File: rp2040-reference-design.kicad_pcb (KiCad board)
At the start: 4 copper layers, 29.5 x 27 mm, 36 parts, among them J2 Conn_01x10_Pin, J3 Conn_01x10_Pin, U1 RP2040, U2 W25Q128JVS, Y1 12mhz ABM8-272-T

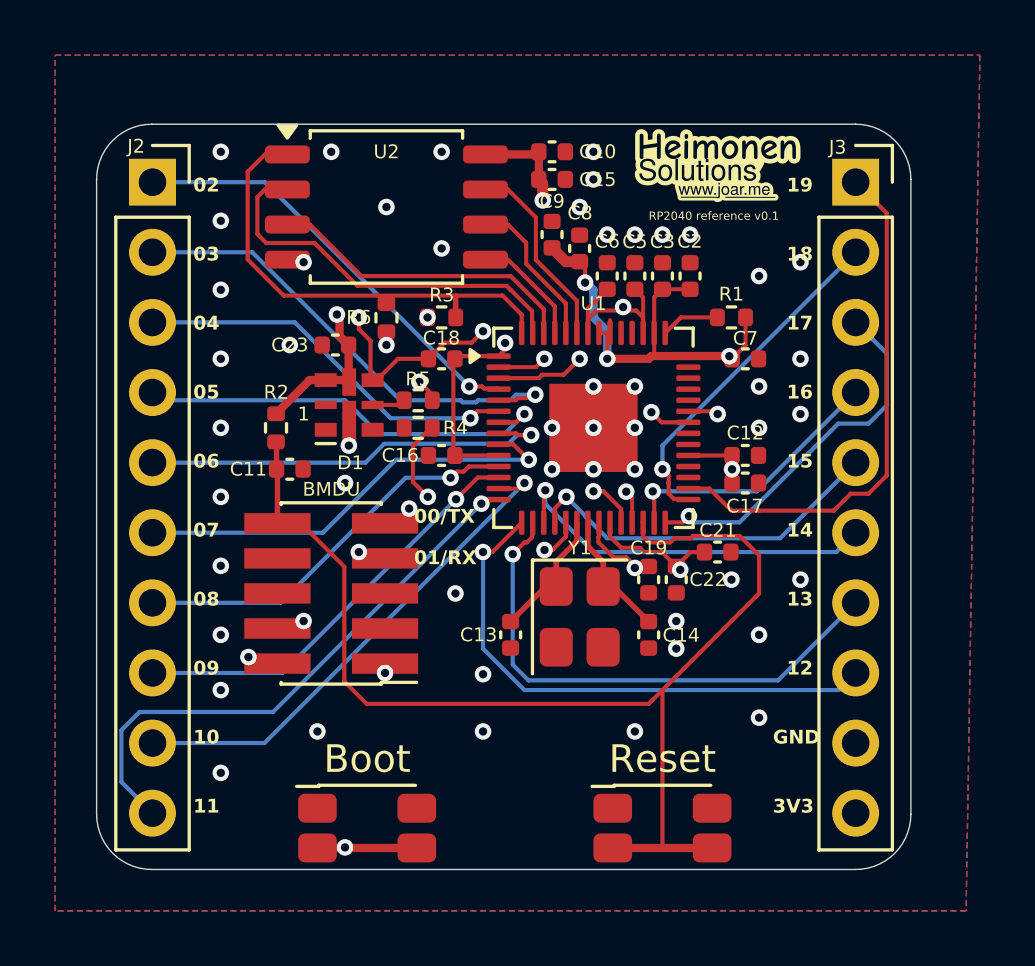
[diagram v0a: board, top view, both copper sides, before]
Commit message: fix: grounded cap
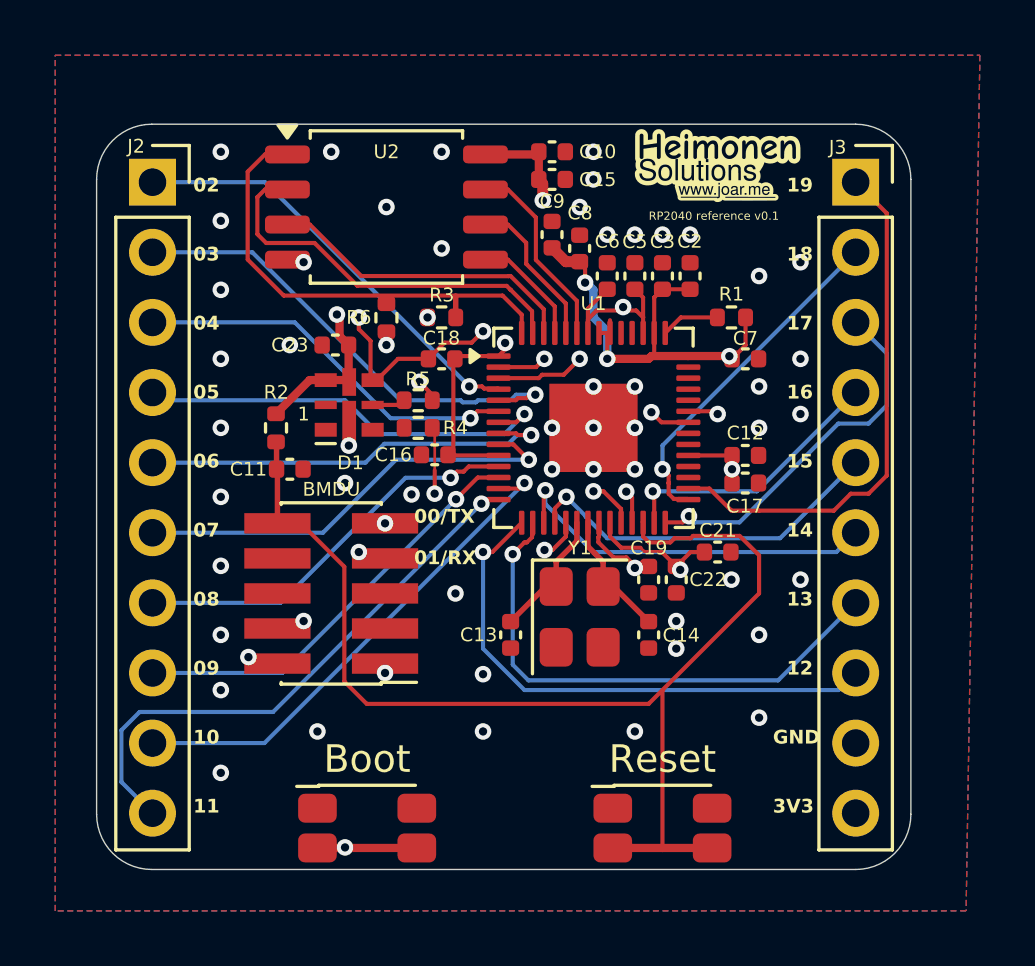
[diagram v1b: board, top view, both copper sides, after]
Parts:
- moved C16 0.25 mm to (120.7, 97.5)
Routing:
- net SDI: track 17.1 -> 16.5 mm
- net GND: vias 53 -> 54
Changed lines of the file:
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@@
 		(descr "SMD3225/4, Crystal, 3.2x2.5mm package, SMD, generated with kicad-footprint-generator make_crystal.py, http://www.txccrystal.com/images/pdf/7m-accuracy.pdf")
 		(property "Reference" "Y1"
-			(at -2.499104 -0.006799 180)
+			(at -2.499104 -0.006799 0)
 			(layer "F.SilkS")
 			(effects
@@
 	(footprint "Capacitor_SMD:C_0402_1005Metric"
 		(layer "F.Cu")
-		(at 121 97.5)
+		(at 120.748977 97.476247)
 		(descr "Capacitor SMD 0402 (1005 Metric), square (rectangular) end terminal, IPC-7351 nominal, (Body size source: IPC-SM-782 page 76, https://www.pcb-3d.com/wordpress/wp-content/uploads/ipc-sm-782a_amendment_1_and_2.pdf), generated with kicad-footprint-generator")
 		(tags "capacitor")
@@
 	)
 	(via
+		(at 119.90973 98.912126)
+		(size 0.6)
+		(drill 0.3)
+		(layers "F.Cu" "B.Cu")
+		(free yes)
+		(net 1)
+	)
+	(via
 		(at 126 88.5)
 		(size 0.6)
@@
 	)
 	(segment
-		(start 118.95 99.96)
-		(end 119.287228 99.96)
-		(width 0.15)
-		(layer "F.Cu")
-		(net 11)
-	)
-	(segment
 		(start 124.420468 94.3)
 		(end 123.0625 94.3)
@@
 		(net 11)
 	)
-	(segment
-		(start 119.287228 99.96)
-		(end 119.822228 99.425)
-		(width 0.15)
-		(layer "F.Cu")
-		(net 11)
-	)
 	(via
-		(at 119.822228 99.425)
+		(at 118.95 99.96)
 		(size 0.6)
 		(drill 0.3)
@@
 	)
 	(segment
-		(start 120.210146 94)
-		(end 119.615742 94.594404)
+		(start 119 99.834256)
+		(end 119 95.210146)
 		(width 0.15)
 		(layer "In1.Cu")
@@
 	)
 	(segment
-		(start 119.615742 94.594404)
-		(end 119.615742 99.218514)
+		(start 118.95 99.884256)
+		(end 119 99.834256)
 		(width 0.15)
 		(layer "In1.Cu")
@@
 	)
 	(segment
-		(start 119.615742 99.218514)
-		(end 119.822228 99.425)
+		(start 118.95 99.96)
+		(end 118.95 99.884256)
 		(width 0.15)
 		(layer "In1.Cu")
@@
 	)
 	(segment
-		(start 124.720468 94)
+		(start 120.210146 94)
+		(end 124.720468 94)
+		(width 0.15)
+		(layer "In1.Cu")
+		(net 11)
+	)
+	(segment
+		(start 119 95.210146)
 		(end 120.210146 94)
 		(width 0.15)
@@
 	)
 	(segment
-		(start 120.66 96.5)
-		(end 120.617806 96.5)
+		(start 129.9375 95.9)
+		(end 130.9 95.9)
 		(width 0.15)
 		(layer "F.Cu")
@@
 	)
 	(segment
-		(start 129.9375 95.9)
-		(end 130.9 95.9)
+		(start 120.748977 96.588977)
+		(end 120.66 96.5)
 		(width 0.15)
 		(layer "F.Cu")
@@
 	)
 	(segment
-		(start 119.964 97.153806)
-		(end 119.964 98.464)
+		(start 120.747189 98.884998)
+		(end 120.747189 98.752811)
 		(width 0.15)
 		(layer "F.Cu")
@@
 	)
 	(segment
-		(start 130.9 95.9)
-		(end 131 96)
+		(start 120.748977 98.751023)
+		(end 120.748977 98.046306)
 		(width 0.15)
 		(layer "F.Cu")
@@
 	)
 	(segment
-		(start 120.617806 96.5)
-		(end 119.964 97.153806)
+		(start 120.748977 98.046306)
+		(end 120.748977 96.588977)
+		(width 0.1)
+		(layer "F.Cu")
+		(net 37)
+	)
+	(segment
+		(start 120.747189 98.752811)
+		(end 120.748977 98.751023)
 		(width 0.15)
 		(layer "F.Cu")
@@
 	)
 	(segment
-		(start 119.964 98.464)
-		(end 120.5 99)
+		(start 130.9 95.9)
+		(end 131 96)
 		(width 0.15)
 		(layer "F.Cu")
@@
 	)
 	(via
-		(at 120.5 99)
+		(at 120.747189 98.884998)
 		(size 0.6)
 		(drill 0.3)
@@
 	)
 	(segment
-		(start 121.323809 99.823809)
-		(end 120.5 99)
+		(start 127.424 97.837412)
+		(end 127.424 97.761412)
 		(width 0.15)
 		(layer "In1.Cu")
@@
 	)
 	(segment
-		(start 131 96)
-		(end 129.576 97.424)
+		(start 120.747189 99.247189)
+		(end 121.323809 99.823809)
 		(width 0.15)
 		(layer "In1.Cu")
@@
 	)
 	(segment
-		(start 127.424 97.837412)
+		(start 120.747189 98.884998)
+		(end 120.747189 99.247189)
+		(width 0.15)
+		(layer "In1.Cu")
+		(net 37)
+	)
+	(segment
+		(start 127.076 99.038591)
 		(end 127.076 98.185412)
 		(width 0.15)
@@
 	)
 	(segment
-		(start 127.076 98.185412)
-		(end 127.076 99.038591)
+		(start 127.761412 97.424)
+		(end 129.576 97.424)
 		(width 0.15)
 		(layer "In1.Cu")
@@
 	)
 	(segment
-		(start 129.576 97.424)
-		(end 127.761412 97.424)
+		(start 126.290782 99.823809)
+		(end 127.076 99.038591)
 		(width 0.15)
 		(layer "In1.Cu")
@@
 	)
 	(segment
-		(start 127.076 99.038591)
-		(end 126.290782 99.823809)
+		(start 127.424 97.761412)
+		(end 127.761412 97.424)
 		(width 0.15)
 		(layer "In1.Cu")
@@
 	)
 	(segment
-		(start 126.290782 99.823809)
-		(end 121.323809 99.823809)
+		(start 129.576 97.424)
+		(end 131 96)
 		(width 0.15)
 		(layer "In1.Cu")
@@
 	)
 	(segment
-		(start 127.424 97.761412)
-		(end 127.424 97.837412)
+		(start 121.323809 99.823809)
+		(end 126.290782 99.823809)
 		(width 0.15)
 		(layer "In1.Cu")
@@
 	)
 	(segment
-		(start 127.761412 97.424)
-		(end 127.424 97.761412)
+		(start 127.076 98.185412)
+		(end 127.424 97.837412)
 		(width 0.15)
 		(layer "In1.Cu")
@@
 		(hatch edge 0.5)
 		(connect_pads yes
-			(clearance 0.15)
+			(clearance 0.1)
 		)
 		(min_thickness 0.25)

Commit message: fix: more stitching
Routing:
- net nRst: track 43.6 -> 45.0 mm
- net SWDCLK: track 14.9 -> 15.4 mm
- net GND: vias 54 -> 61
